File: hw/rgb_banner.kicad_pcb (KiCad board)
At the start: 2 copper layers, 96 x 56 mm, 90 parts, among them P1 +5V, P2 GND, P3 DIN, P4 +5V, P5 GND, P6 DOUT, U1 WS2812B, U10 WS2812B, U11 WS2812B, U12 WS2812B, U13 WS2812B, U14 WS2812B, U15 WS2812B, U16 WS2812B, U17 WS2812B, U18 WS2812B, U19 WS2812B, U2 WS2812B, U20 WS2812B, U21 WS2812B, U22 WS2812B, U23 WS2812B, U24 WS2812B, U25 WS2812B, U26 WS2812B, U27 WS2812B, U28 WS2812B, U29 WS2812B, U3 WS2812B, U30 WS2812B, U31 WS2812B, U32 WS2812B, U33 WS2812B, U34 WS2812B, U35 WS2812B, U36 WS2812B, U37 WS2812B, U38 WS2812B, U39 WS2812B, U4 WS2812B, U40 WS2812B, U41 WS2812B, U42 WS2812B, U43 WS2812B, U44 WS2812B, U45 WS2812B, U46 WS2812B, U47 WS2812B, U48 WS2812B, U49 WS2812B, U5 WS2812B, U50 WS2812B, U51 WS2812B, U52 WS2812B, U53 WS2812B, U54 WS2812B, U55 WS2812B, U56 WS2812B, U57 WS2812B, U58 WS2812B, U59 WS2812B, U6 WS2812B, U60 WS2812B, U61 WS2812B, U62 WS2812B, U63 WS2812B, U64 WS2812B, U65 WS2812B, U66 WS2812B, U67 WS2812B, U68 WS2812B, U69 WS2812B, U7 WS2812B, U70 WS2812B, U71 WS2812B, U72 WS2812B, U73 WS2812B, U74 WS2812B, U75 WS2812B, U76 WS2812B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

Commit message: work on pcb
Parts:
- turned U57 to 180 degrees
- turned U58 to 180 degrees
- turned U59 to 180 degrees
- turned U60 to 180 degrees
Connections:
- U11 pad 1: Net-(U11-Pad1) -> /+5V
- U23 pad 3: Net-(U23-Pad3) -> /gnd
- U35 pad 1: Net-(U35-Pad1) -> /+5V
- U47 pad 3: Net-(U47-Pad3) -> /gnd
- U59 pad 1: Net-(U59-Pad1) -> /+5V
- U71 pad 3: Net-(U71-Pad3) -> /gnd
- U83 pad 1: Net-(U83-Pad1) -> /+5V
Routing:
- net /gnd: track 0.00 -> 194.9 mm
- net /+5V: track 36.3 -> 179.5 mm
- net (no net): track 0.00 -> 62.0 mm, vias 0 -> 6
- net Net-(U61-Pad2): track 0.00 -> 13.0 mm, vias 0 -> 2
- net Net-(U37-Pad2): track 0.00 -> 13.0 mm, vias 0 -> 2
- net Net-(U13-Pad2): track 0.00 -> 13.0 mm, vias 0 -> 2
- net Net-(U12-Pad2): track 0.00 -> 13.0 mm, vias 0 -> 2
- net Net-(U60-Pad2): track 0.00 -> 13.0 mm, vias 0 -> 2
- net Net-(U36-Pad2): track 0.00 -> 13.0 mm, vias 0 -> 2
- net Net-(U16-Pad4): track 0.00 -> 8.87 mm
- net Net-(U70-Pad4): track 0.00 -> 5.70 mm
- net Net-(U77-Pad2): track 0.00 -> 5.27 mm
- net Net-(U8-Pad2): track 0.00 -> 4.48 mm
- net Net-(U11-Pad2): track 0.00 -> 4.48 mm
- net Net-(U10-Pad4): track 0.00 -> 4.48 mm
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- removed copper zone on F.Cu, net /digit1/+5V

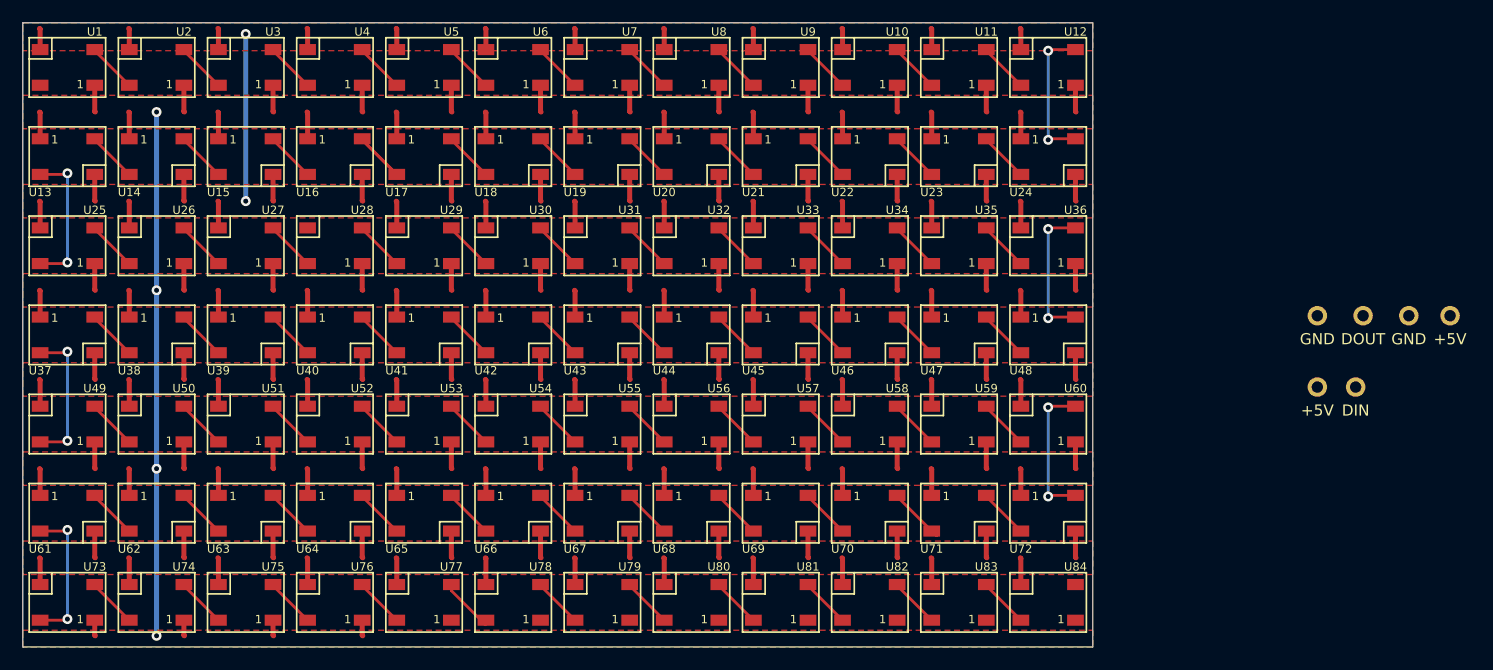
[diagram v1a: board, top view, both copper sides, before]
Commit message: add gerbers, update the mockups a bit
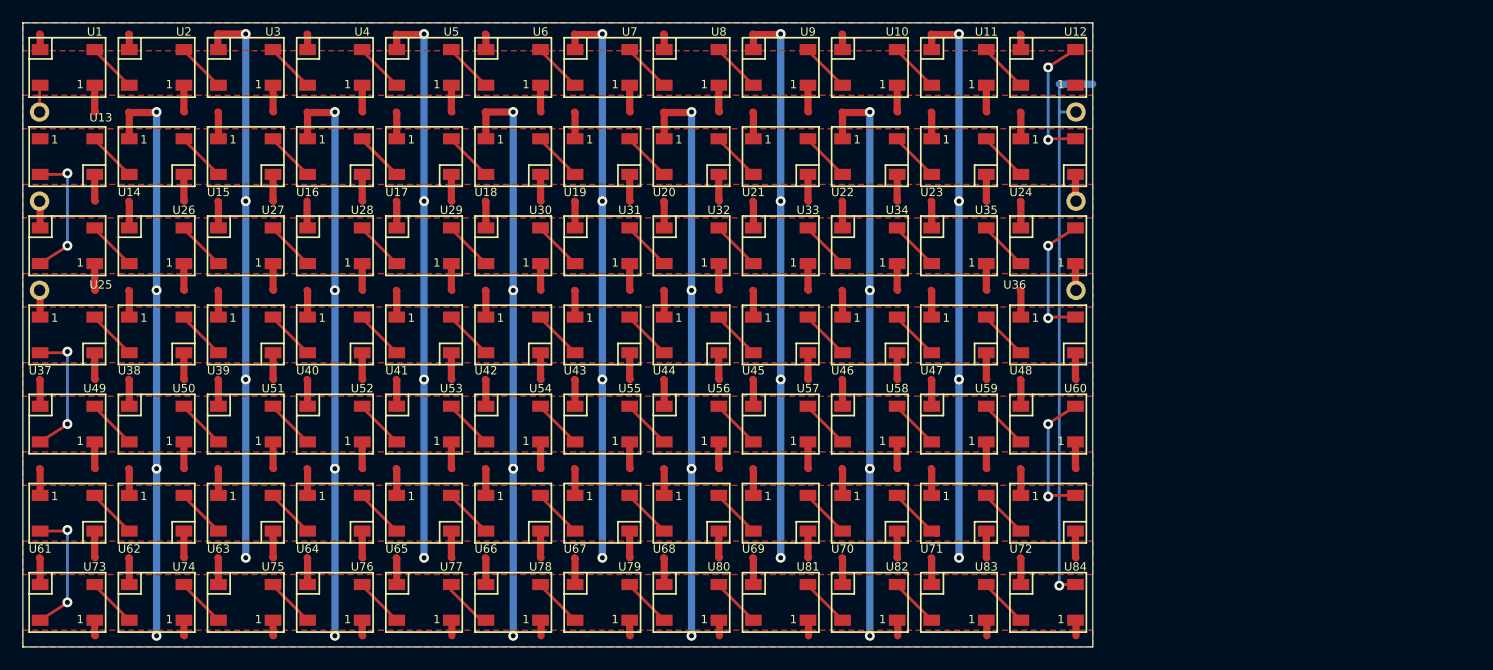
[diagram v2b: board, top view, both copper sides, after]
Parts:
- moved P3 120.6 mm to (69.5, 60.0)
- moved P2 115.1 mm to (69.5, 68.0)
- moved P1 115.0 mm to (69.5, 76.0)
- moved P4 33.6 mm to (162.5, 76.0)
- moved P6 31.6 mm to (162.5, 60.0)
- moved P5 31.6 mm to (162.5, 68.0)
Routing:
- net /+5V: track 179.5 -> 433.9 mm, vias 0 -> 20
- net /gnd: track 194.9 -> 438.7 mm, vias 0 -> 20
- net (no net): track 62.0 -> 0.00 mm, vias 6 -> 0
- net /d_out: track 0.00 -> 51.1 mm, vias 0 -> 1
- net /d_in: track 0.00 -> 2.49 mm
- net Net-(U61-Pad2): track 13.0 -> 11.9 mm
- net Net-(U37-Pad2): track 13.0 -> 11.9 mm
- net Net-(U13-Pad2): track 13.0 -> 11.9 mm
- net Net-(U60-Pad2): track 13.0 -> 11.9 mm
- net Net-(U36-Pad2): track 13.0 -> 11.9 mm
- net Net-(U12-Pad2): track 13.0 -> 11.9 mm
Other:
- net class phatty: trace_width 0.45 -> 0.65

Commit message: add silks to the back
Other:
- board text added: "RGB Banner 2 Digit Module https://github.com/noahp/rgb_banner PCB Rev 0.1"
